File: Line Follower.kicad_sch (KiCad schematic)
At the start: 13 parts, among them J1 Conn_01x11, J2 Conn_01x08, J3 Conn_01x04, J4 Conn_01x06, J5 Conn_01x06, U1 Teensy4.1, U2 D42V55F5 5V Voltage Regulator, U3 TB67H420FTG Dual Motor Driver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, U4 Big MOSFET Slide Switch with 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

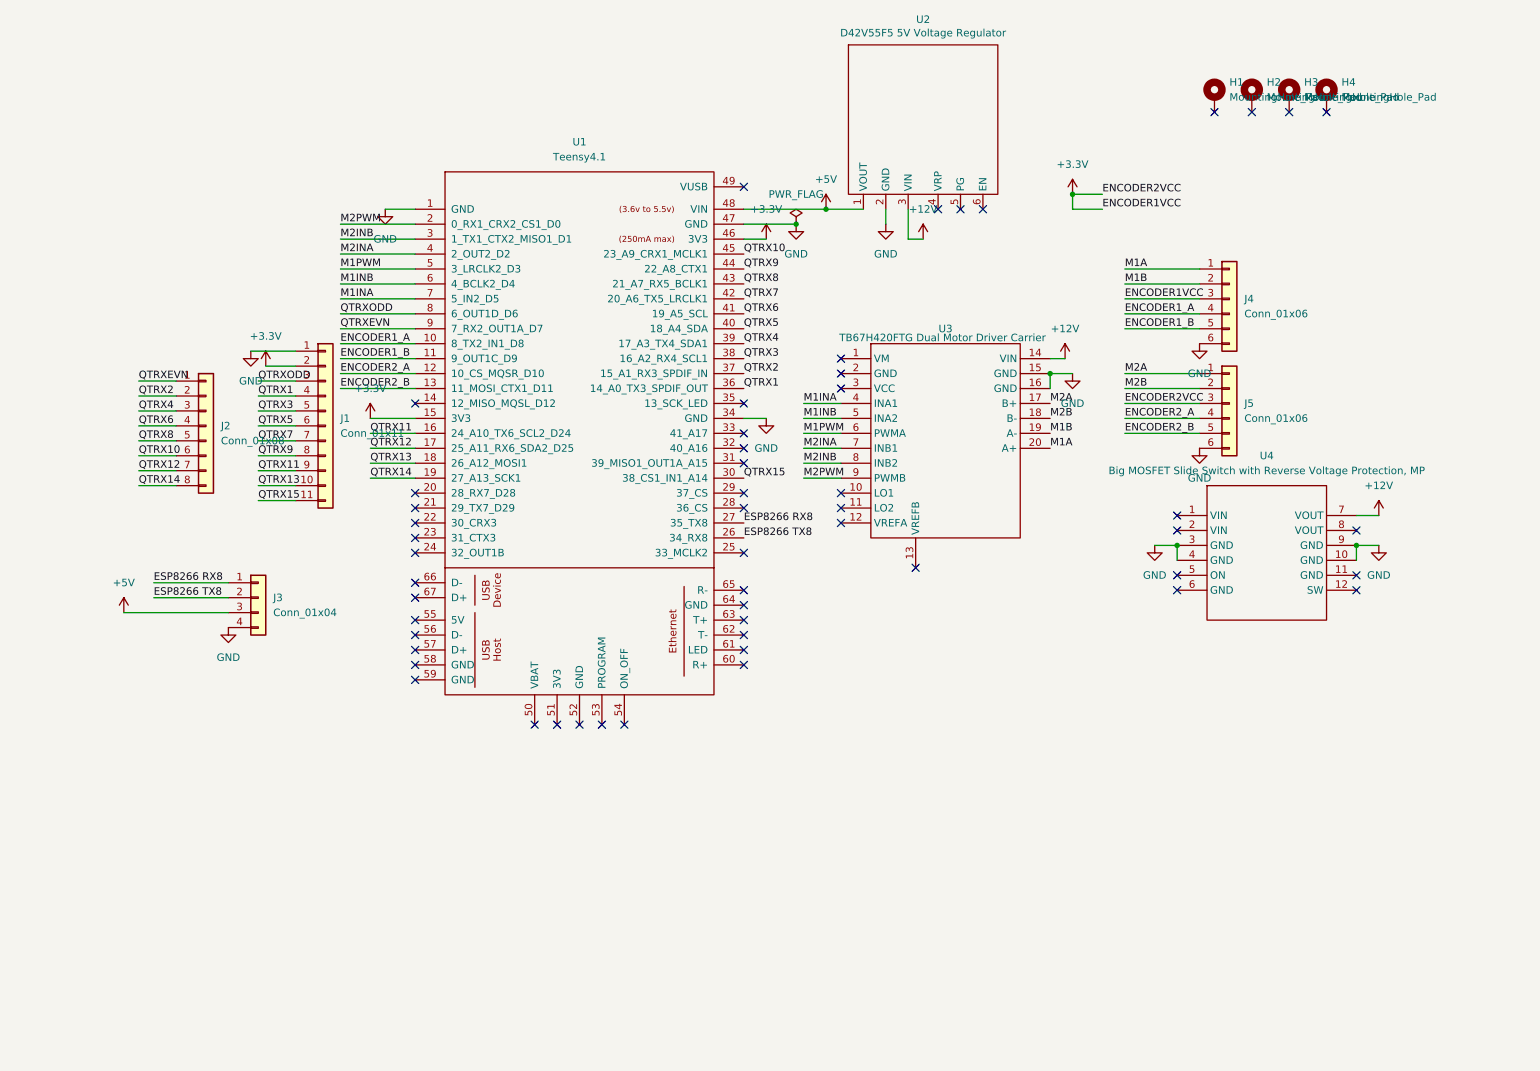
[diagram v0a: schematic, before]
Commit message: Add PCB routing rules and lock files for Line Follower project
- Created a new freerouting.rules file with detailed autorouting settings, layer rules, via definitions, and clearance classes for the PCB design.
- Added lock files for both the PCB and schematic to track user session information.
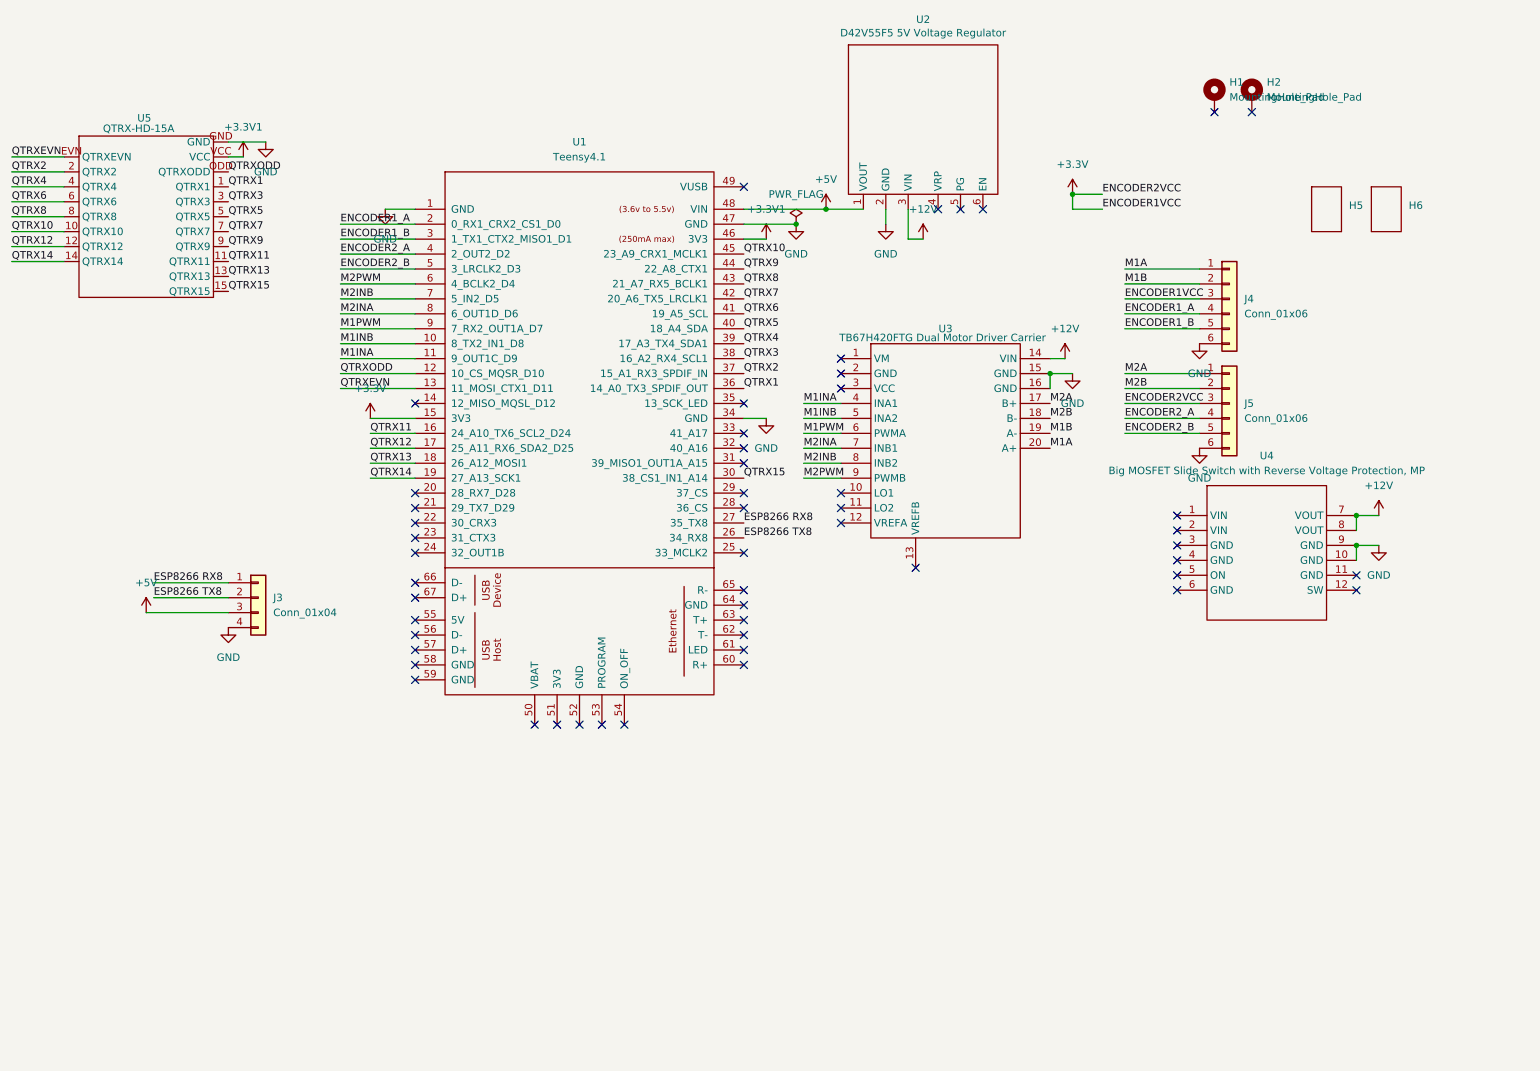
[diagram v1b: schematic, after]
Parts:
- removed H3, H4: MountingHole_Pad, MountingHole:MountingHole_3.2mm_M3_Pad_Via, symbol Mechanical:MountingHole_Pad
- removed J1: Conn_01x11, Connector_PinSocket_2.54mm:PinSocket_1x11_P2.54mm_Vertical, symbol Connector_Generic:Conn_01x11
- removed J2: Conn_01x08, Connector_PinSocket_2.54mm:PinSocket_1x08_P2.54mm_Vertical, symbol Connector_Generic:Conn_01x08
- added H5, H6: ~, Pololu:Pololu Extended Motor Bracket, symbol Pololu:N20_Extended_Motor_Bracket
- added U5: QTRX-HD-15A, Pololu:QTRX-HD-15A, symbol Pololu:QTRX-HD-15A
- H1, H2: footprint MountingHole:MountingHole_3.2mm_M3_Pad_Via -> MountingHole:MountingHole_2.2mm_M2_Pad_Via
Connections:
- net +12V: now also U4.8 (VOUT)
- net +3.3V: no longer U1.46 (3V3)
- net ENCODER1_A: now also U1.2 (0_RX1_CRX2_CS1_D0); no longer U1.10 (8_TX2_IN1_D8)
- net ENCODER1_B: now also U1.3 (1_TX1_CTX2_MISO1_D1); no longer U1.11 (9_OUT1C_D9)
- net ENCODER2_A: now also U1.4 (2_OUT2_D2); no longer U1.12 (10_CS_MQSR_D10)
- net ENCODER2_B: now also U1.5 (3_LRCLK2_D3); no longer U1.13 (11_MOSI_CTX1_D11)
- net GND: now also U5.GND; no longer U4.3 (GND), U4.4 (GND)
- net M1INA: now also U1.11 (9_OUT1C_D9); no longer U1.7 (5_IN2_D5)
- net M1INB: now also U1.10 (8_TX2_IN1_D8); no longer U1.6 (4_BCLK2_D4)
- net M1PWM: now also U1.9 (7_RX2_OUT1A_D7); no longer U1.5 (3_LRCLK2_D3)
- net M2INA: now also U1.8 (6_OUT1D_D6); no longer U1.4 (2_OUT2_D2)
- net M2INB: now also U1.7 (5_IN2_D5); no longer U1.3 (1_TX1_CTX2_MISO1_D1)
- net M2PWM: now also U1.6 (4_BCLK2_D4); no longer U1.2 (0_RX1_CRX2_CS1_D0)
- net QTRX1: now also U5.1 (QTRX1)
- net QTRX10: now also U5.10 (QTRX10)
- net QTRX11: now also U5.11 (QTRX11)
- net QTRX12: now also U5.12 (QTRX12)
- net QTRX13: now also U5.13 (QTRX13)
- net QTRX14: now also U5.14 (QTRX14)
- net QTRX15: now also U5.15 (QTRX15)
- net QTRX2: now also U5.2 (QTRX2)
- net QTRX3: now also U5.3 (QTRX3)
- net QTRX4: now also U5.4 (QTRX4)
- net QTRX5: now also U5.5 (QTRX5)
- net QTRX6: now also U5.6 (QTRX6)
- net QTRX7: now also U5.7 (QTRX7)
- net QTRX8: now also U5.8 (QTRX8)
- net QTRX9: now also U5.9 (QTRX9)
- net QTRXEVN: now also U1.13 (11_MOSI_CTX1_D11), U5.EVN (QTRXEVN); no longer U1.9 (7_RX2_OUT1A_D7)
- net QTRXODD: now also U1.12 (10_CS_MQSR_D10), U5.ODD (QTRXODD); no longer U1.8 (6_OUT1D_D6)
- new net +3.3V1: U1.46 (3V3), U5.VCC
- no-connect marks 53 -> 52

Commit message: Version1.0 QTRX-HD15A
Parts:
- removed J3: Conn_01x04, Connector_PinSocket_2.54mm:PinSocket_1x04_P2.54mm_Vertical, symbol Connector_Generic:Conn_01x04
- removed U3: TB67H420FTG Dual Motor Driver Carrier, Pololu:TB67H420FTG Dual Motor Driver Carrier, symbol Pololu:TB67H420FTG_Dual_Motor_Driver_Carrier
- added C1, C2, C3, C4, C7, C8, C9: 0.1uF, Capacitor_SMD:C_0805_2012Metric_Pad1.18x1.45mm_HandSolder, symbol Device:C_Small_US
- added C10, C5: 22uF, Capacitor_SMD:C_0805_2012Metric_Pad1.18x1.45mm_HandSolder, symbol Device:C_Small_US
- added C6: 470uF, Capacitor_THT:CP_Radial_D8.0mm_P3.50mm, symbol Device:C_Polarized_Small_US
- added U3: ESP32-C3_SUPERMINI_TH, ESP32-C3_SUPERMINI_TH:MODULE_ESP32-C3_SUPERMINI_TH, symbol ESP32-C3_SUPERMINI_TH:ESP32-C3_SUPERMINI_TH
- added U6: TB6612FNG BreakoutBoard, Pololu:MODULE_ROB-14450, symbol ROB-14450:ROB-14450
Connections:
- net +12V: now also C6.1, U6.1 (VM)
- net +3.3V: now also U6.2 (VCC)
- net +3.3V1: now also C1.1
- net +5V: now also C10.2, C2.2, C3.2, C4.2, C5.2, C7.2, C8.2, C9.2, U3.5V
- net GND: now also C1.2, C10.1, C2.1, C3.1, C4.1, C5.1, C6.2, C7.1, C8.1, C9.1, U3.G (GND), U6.3 (GND), U6.8 (GND), U6.9 (GND); no longer U4.10 (GND)
- net M1A: now also U6.4 (A01)
- net M1B: now also U6.5 (A02)
- net M1INA: now also U1.12 (10_CS_MQSR_D10), U6.14 (AI1); no longer U1.11 (9_OUT1C_D9)
- net M1INB: now also U1.11 (9_OUT1C_D9), U6.15 (AI2); no longer U1.10 (8_TX2_IN1_D8)
- net M1PWM: now also U1.10 (8_TX2_IN1_D8), U6.16 (PWMA); no longer U1.9 (7_RX2_OUT1A_D7)
- net M2A: now also U6.7 (B01)
- net M2B: now also U6.6 (B02)
- net M2INA: now also U1.9 (7_RX2_OUT1A_D7), U6.12 (BI1); no longer U1.8 (6_OUT1D_D6)
- net M2INB: now also U1.8 (6_OUT1D_D6), U6.11 (BI2); no longer U1.7 (5_IN2_D5)
- net M2PWM: now also U6.10 (PWMB)
- net QTRXEVN: now also U1.14 (12_MISO_MQSL_D12); no longer U1.13 (11_MOSI_CTX1_D11)
- net QTRXODD: now also U1.13 (11_MOSI_CTX1_D11); no longer U1.12 (10_CS_MQSR_D10)
- net STBY: now reaches U1.20 (28_RX7_D28)
- net STBY: now also U6.13 (STBY)
- net ESP8266 RX8 renamed ESP32 RX8
- net ESP32 RX8: now also U3.20 (GPIO20)
- net ESP8266 TX8 renamed ESP32 TX8
- net ESP32 TX8: now also U3.21 (GPIO21)
- no-connect marks 52 -> 57
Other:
- note added: "12V - 5V Voltage Regulator"
- note added: "ESP32 C3 SUPERMINI MICROCONTROLLER DATA VIA WIFI"
- note added: "MOSFET SLIDE SWITCH 12V LIPO BATTERY TO SLIDE SWITCH"
- note added: "MOTOR ENCODER FEMALE PINS"
- note added: "QTRX-HD15A ANALOG SENSOR"
- note added: "TB6612FNG MOTOR DRIVER"
- note added: "TEENSY 4.1 MAIN MICROCONTROLLER"
- title: (none) -> Teensy 4.1 Line Follower
- moved on the sheet: H1, H2, H5, H6, J4, J5, U1, U2, U4, U5
